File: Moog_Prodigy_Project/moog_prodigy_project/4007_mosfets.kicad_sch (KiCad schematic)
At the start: 24 parts, among them Q110 BC327, Q111 BC327, SW101 FINAL DECAY SWITCH, SW102 FINAL DECAY SWITCH, U103 OPA184, U104 OPA184

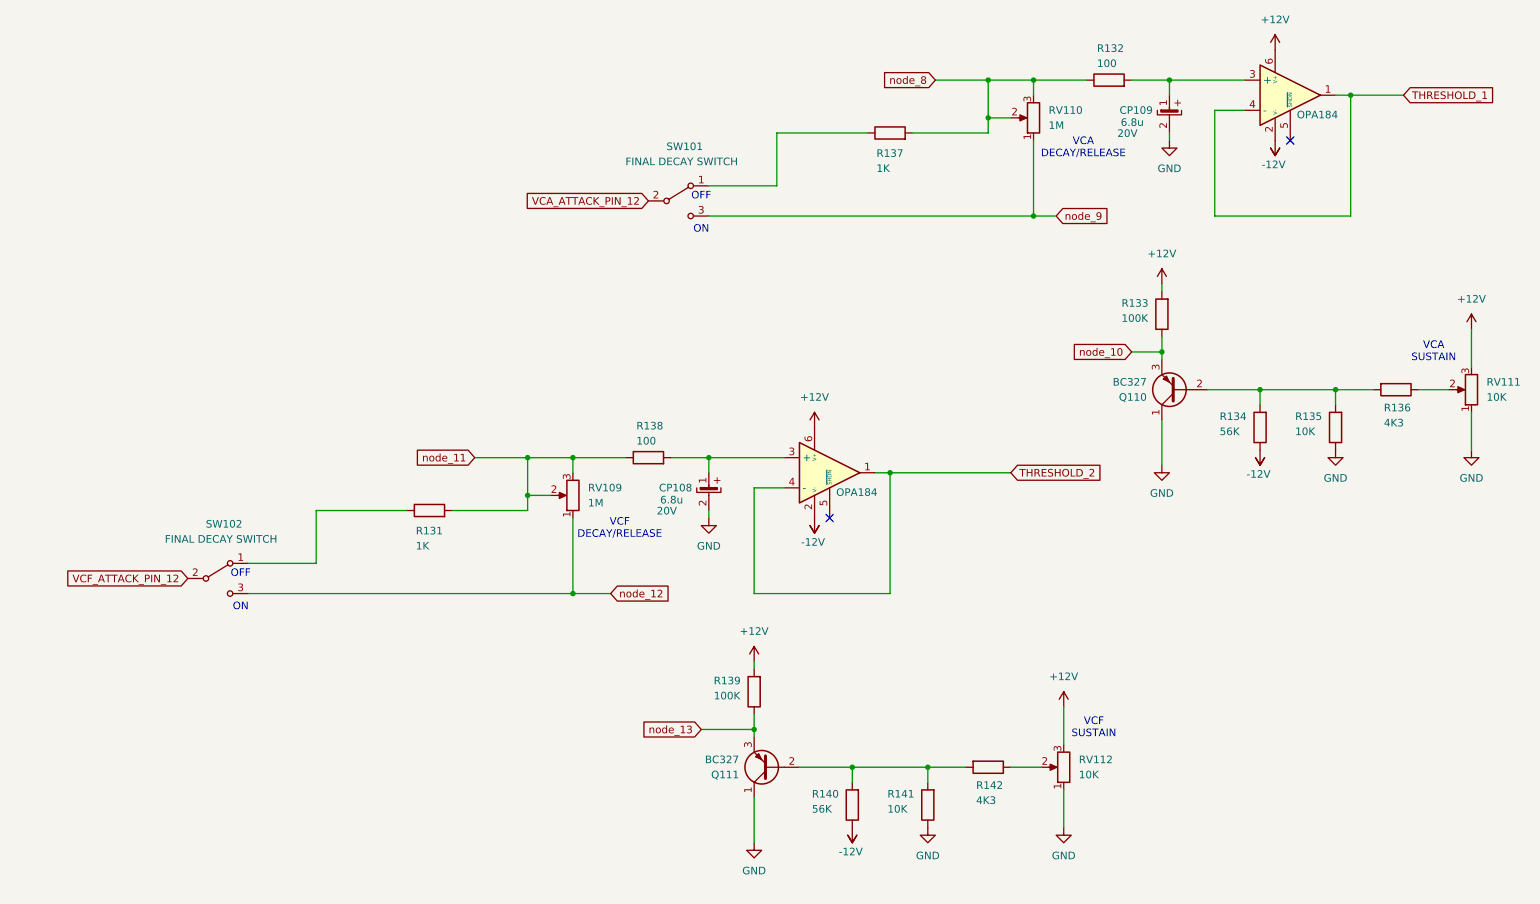
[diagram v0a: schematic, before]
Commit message: problemi sa ca3096, multiplicirani footprintovi
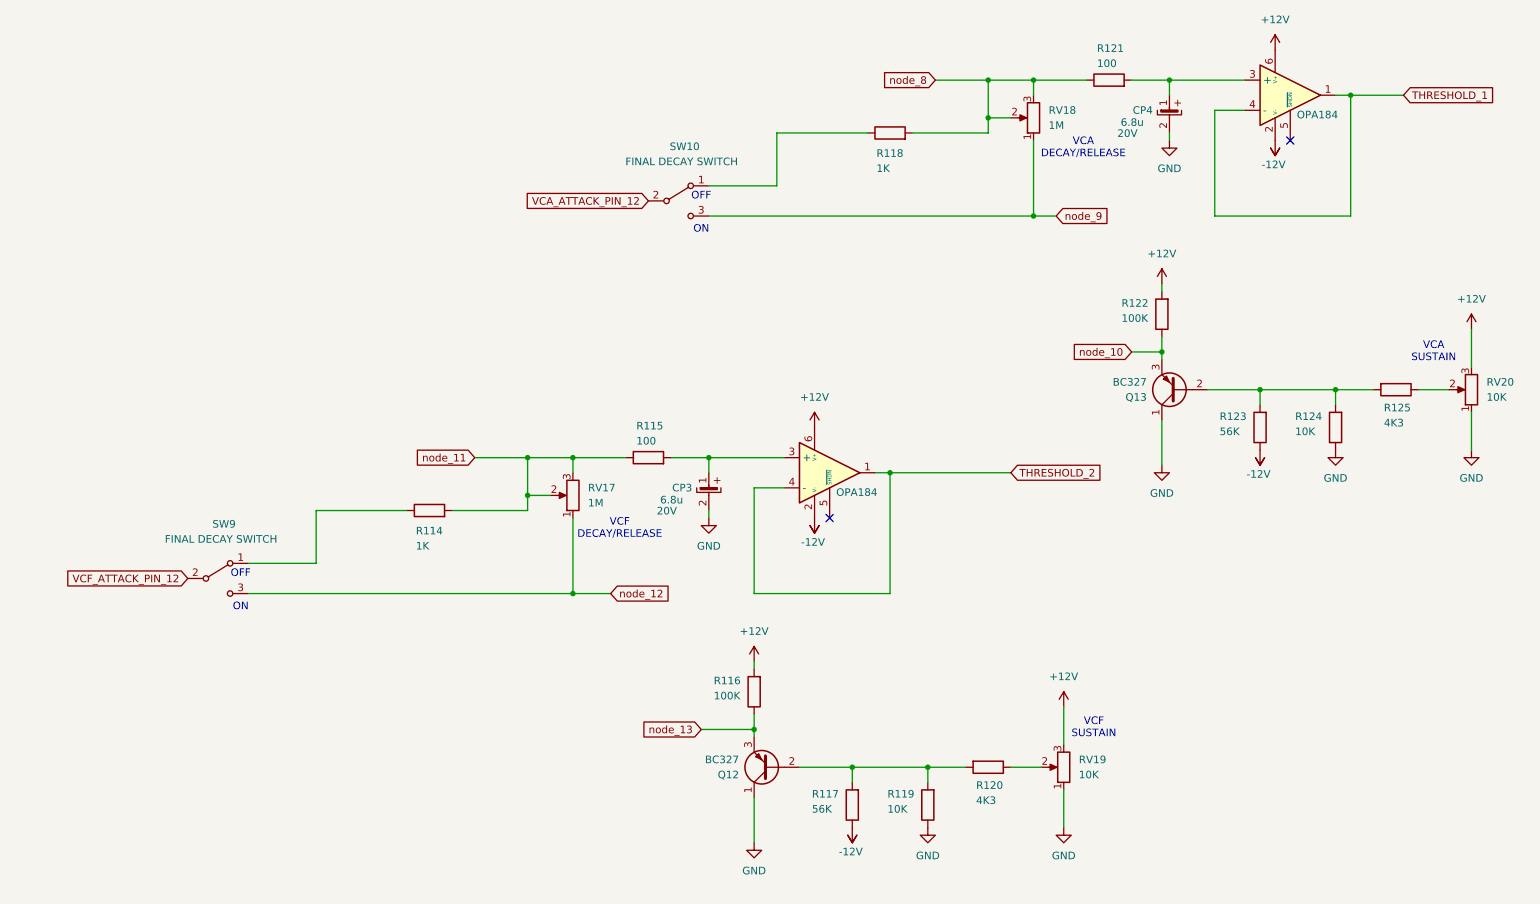
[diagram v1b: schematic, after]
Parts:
- renumbered CP108 to CP3, CP109 to CP4, Q111 to Q12, Q110 to Q13, R131 to R114, R138 to R115, R139 to R116, R140 to R117, R137 to R118, R141 to R119, R142 to R120, R132 to R121, R133 to R122, R134 to R123, R135 to R124, R136 to R125, RV109 to RV17, RV110 to RV18, RV112 to RV19, RV111 to RV20, SW101 to SW10, SW102 to SW9, U104 to U18, U103 to U19

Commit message: Fix 1 nakon review-a 27.05.2026
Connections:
- net GND: now also Q12. (E), Q13. (E); no longer Q12.1 (C), Q13.1 (C)
- net node_10: now also Q13. (E); no longer Q13.3 (E)
- net node_13: now also Q12. (E); no longer Q12.3 (E)
- net at R117.2, R119.2, R120.2: now also Q12. (E); no longer Q12.2 (B)
- net at R123.2, R124.2, R125.2: now also Q13. (E); no longer Q13.2 (B)
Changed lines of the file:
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@@
 	(generator_version "9.0")
 	(paper "A4")
+	(title_block
+		(rev "Marjan Urekar")
+		(comment 1 "Fakultet tehničkih nauka")
+		(comment 2 "Univerzitet u Novom Sadu")
+		(comment 3 "Merno-Informacioni sistemi")
+	)
 	(text "VCF\nDECAY/RELEASE"
 		(exclude_from_sim no)
@@
 	)
 	(symbol
+		(lib_name "BC556_1")
 		(lib_id "Transistor_BJT:BC556")
 		(at 208.28 78.74 180)
@@
 			)
 		)
-		(pin "1"
-		)
-		(pin "3"
-		)
-		(pin "2"
+		(pin ""
+		)
+		(pin ""
+		)
+		(pin ""
 		)
 		(instances
@@
 			)
 		)
-		(pin "1"
-		)
-		(pin "3"
-		)
-		(pin "2"
+		(pin ""
+		)
+		(pin ""
+		)
+		(pin ""
 		)
 		(instances

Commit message: Latest checkpoints update 05.06.2026
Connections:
- net GND: now also CP3., CP4.; no longer CP3.2, CP4.2
- net at R115.2, U18.3 (+): now also CP3.; no longer CP3.1
- net at R121.2, U19.3 (+): now also CP4.; no longer CP4.1
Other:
- moved on the sheet: Q12, Q13, R114, R115, R116, R117, R118, R119, R120, R121, R122, R123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

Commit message: 27.06.2026 - dodavanje izmena sa konsultacija
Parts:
- added C77, C78, C79, C80: 100n, Capacitor_THT:CP_Radial_D5.0mm_P2.50mm, symbol Device:C
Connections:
- net +12V: now also C77.2, C79.2
- net -12V: now also C78.2, C80.2
- net GND: now also C77.1, C78.1, C79.1, C80.1
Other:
- note added: "NAPOMENA Kondenzatori: C77,C78,C79,C80 su vrednosti 100n i oni su kvalitetniji"
